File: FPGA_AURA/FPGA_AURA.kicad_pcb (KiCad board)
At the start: 8 copper layers, 50 x 50 mm, 147 parts, among them J1 TF-CARD_H1.8, J100 USB_C_Receptacle_USB2.0_16P, J101 XT30PW-M, J2 532617004, J3 532617007, J4 532617004, U1 XC7A35T-2FTG256C, U2 W25Q256JVEIQ, U200 ADP5014, U3 FT2232HQ, U4 TPS51200DRCR, U5 USBLC6-2SC6, U500 MT41K128M16JT-125_IT_K, U6 93LC56BT-I_SN, Y1 12MHz

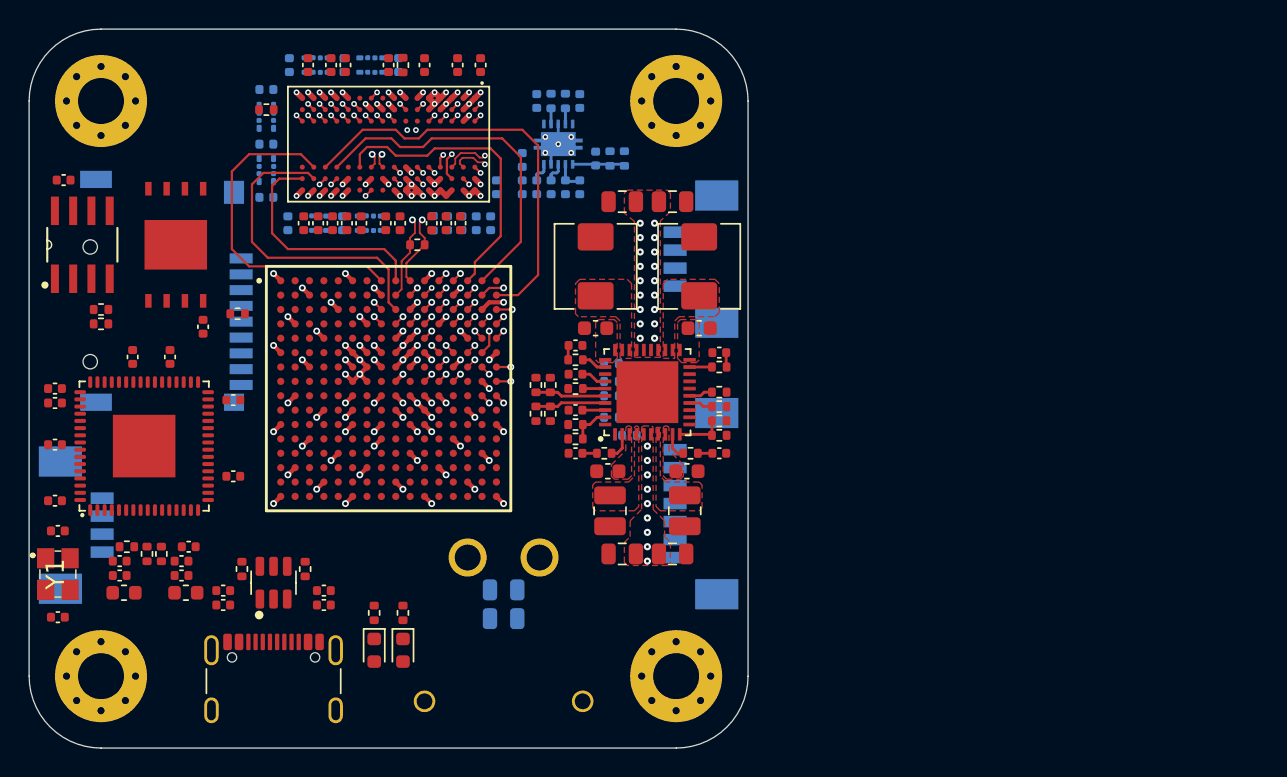
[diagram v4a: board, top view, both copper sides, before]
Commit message: Changing stackup to 10 layers and connectors change
Development has been slow due to SI concerns with 8 layers so changing the layer count to 10 will simplify design. The picoblade/SD connector(s) are large and not high speed, so a high speed mezzanine will be used to go to a daughter board with the picoblade connectors and SD card, or other devices/protocols e.g. ADCs, COAX, IMUs, etc.
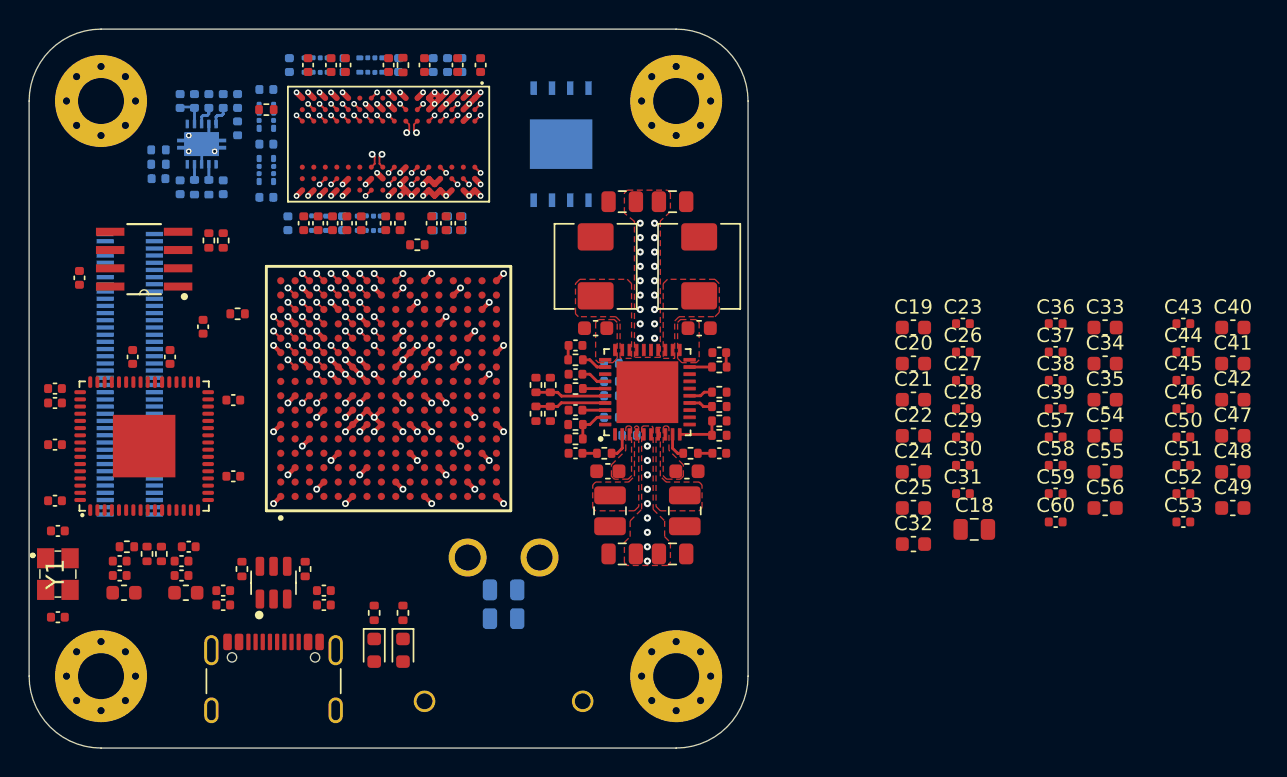
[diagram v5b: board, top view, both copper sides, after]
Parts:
- removed J2, J4: 532617004, 532617004:532617004
- removed J3: 532617007, 532617007:532617007
- added C18: 100u, Capacitor_SMD:C_0805_2012Metric, F.Cu at (165.7, 84.8)
- added C19: 4u7, Capacitor_SMD:C_0603_1608Metric, F.Cu at (161.5, 70.8)
- added C20: 4u7, Capacitor_SMD:C_0603_1608Metric, F.Cu at (161.5, 73.3)
- added C21: 4u7, Capacitor_SMD:C_0603_1608Metric, F.Cu at (161.5, 75.8)
- added C22: 4u7, Capacitor_SMD:C_0603_1608Metric, F.Cu at (161.5, 78.3)
- added C23: 470n, Capacitor_SMD:C_0402_1005Metric, F.Cu at (164.9, 70.5)
- added C24: 4u7, Capacitor_SMD:C_0603_1608Metric, F.Cu at (161.5, 80.8)
- added C25: 47, Capacitor_SMD:C_0603_1608Metric, F.Cu at (161.5, 83.3)
- added C26: 470n, Capacitor_SMD:C_0402_1005Metric, F.Cu at (164.9, 72.5)
- added C27: 470n, Capacitor_SMD:C_0402_1005Metric, F.Cu at (164.9, 74.4)
- added C28: 470n, Capacitor_SMD:C_0402_1005Metric, F.Cu at (164.9, 76.4)
- added C29: 470n, Capacitor_SMD:C_0402_1005Metric, F.Cu at (164.9, 78.4)
- added C30: 470n, Capacitor_SMD:C_0402_1005Metric, F.Cu at (164.9, 80.3)
- added C31: 470n, Capacitor_SMD:C_0402_1005Metric, F.Cu at (164.9, 82.3)
- added C32: 47, Capacitor_SMD:C_0603_1608Metric, F.Cu at (161.5, 85.8)
- added C33: 47, Capacitor_SMD:C_0603_1608Metric, F.Cu at (174.8, 70.8)
- added C34: 4u7, Capacitor_SMD:C_0603_1608Metric, F.Cu at (174.8, 73.3)
- added C35: 4u7, Capacitor_SMD:C_0603_1608Metric, F.Cu at (174.8, 75.8)
- added C36: 470n, Capacitor_SMD:C_0402_1005Metric, F.Cu at (171.4, 70.5)
- added C37: 470n, Capacitor_SMD:C_0402_1005Metric, F.Cu at (171.4, 72.5)
- added C38: 470n, Capacitor_SMD:C_0402_1005Metric, F.Cu at (171.4, 74.4)
- added C39: 470n, Capacitor_SMD:C_0402_1005Metric, F.Cu at (171.4, 76.4)
- added C40: 47, Capacitor_SMD:C_0603_1608Metric, F.Cu at (183.7, 70.8)
- added C41: 4u7, Capacitor_SMD:C_0603_1608Metric, F.Cu at (183.7, 73.3)
- added C42: 4u7, Capacitor_SMD:C_0603_1608Metric, F.Cu at (183.7, 75.8)
- added C43: 470n, Capacitor_SMD:C_0402_1005Metric, F.Cu at (180.3, 70.5)
- added C44: 470n, Capacitor_SMD:C_0402_1005Metric, F.Cu at (180.3, 72.5)
- added C45: 470n, Capacitor_SMD:C_0402_1005Metric, F.Cu at (180.3, 74.4)
- added C46: 470n, Capacitor_SMD:C_0402_1005Metric, F.Cu at (180.3, 76.4)
- added C47: 47, Capacitor_SMD:C_0603_1608Metric, F.Cu at (183.7, 78.3)
- added C48: 4u7, Capacitor_SMD:C_0603_1608Metric, F.Cu at (183.7, 80.8)
- added C49: 4u7, Capacitor_SMD:C_0603_1608Metric, F.Cu at (183.7, 83.3)
- added C50: 470n, Capacitor_SMD:C_0402_1005Metric, F.Cu at (180.3, 78.4)
- added C51: 470n, Capacitor_SMD:C_0402_1005Metric, F.Cu at (180.3, 80.3)
- added C52: 470n, Capacitor_SMD:C_0402_1005Metric, F.Cu at (180.3, 82.3)
- added C53: 470n, Capacitor_SMD:C_0402_1005Metric, F.Cu at (180.3, 84.3)
- added C54: 47, Capacitor_SMD:C_0603_1608Metric, F.Cu at (174.8, 78.3)
- added C55: 4u7, Capacitor_SMD:C_0603_1608Metric, F.Cu at (174.8, 80.8)
- added C56: 4u7, Capacitor_SMD:C_0603_1608Metric, F.Cu at (174.8, 83.3)
- added C57: 470n, Capacitor_SMD:C_0402_1005Metric, F.Cu at (171.4, 78.4)
- added C58: 470n, Capacitor_SMD:C_0402_1005Metric, F.Cu at (171.4, 80.3)
- added C59: 470n, Capacitor_SMD:C_0402_1005Metric, F.Cu at (171.4, 82.3)
- added C60: 470n, Capacitor_SMD:C_0402_1005Metric, F.Cu at (171.4, 84.3)
- J1: value TF-CARD_H1.8 -> ST5-40-1.00-L-D-P-TR; footprint TF-CARD_H1_8:TFCARDH18 -> ST5-40-1.00-L-D-P-TR:ST5-40-1.00-L-D-P-TR
- U2: moved to B.Cu
- moved R222 32.4 mm to (109.0, 58.4), turned to 0 degrees
- moved R221 31.4 mm to (109.0, 59.4), turned to 180 degrees
- moved C216 30.4 mm to (109.0, 60.4), turned to 180 degrees
- moved C217 28.4 mm to (110.5, 55.0), turned to 90 degrees
- moved C221 28.4 mm to (110.5, 61.0), turned to -90 degrees
- moved U2 27.7 mm to (137.0, 58.0)
- moved C218 26.5 mm to (111.5, 55.0), turned to 90 degrees
- moved R223 26.5 mm to (111.5, 61.0), turned to 90 degrees
- moved U4 24.8 mm to (112.0, 58.0), turned to -90 degrees
- moved C215 24.5 mm to (112.5, 55.0), turned to 90 degrees
- moved R220 24.5 mm to (112.5, 61.0), turned to 90 degrees
- moved C214 22.6 mm to (113.5, 61.0), turned to -90 degrees
- moved C219 22.6 mm to (113.5, 55.0), turned to 90 degrees
- moved C222 20.7 mm to (114.5, 55.0), turned to 90 degrees
- moved C508 19.9 mm to (114.5, 56.9), turned to -90 degrees
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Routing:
- net DDR3_ODT: track 37.4 -> 1.27 mm
- net DDR3_CS: track 36.0 -> 1.27 mm
- net DDR3_A2: track 35.9 -> 1.27 mm
- net DDR3_DQ12: track 32.3 -> 1.27 mm
- net DDR3_WE: track 30.7 -> 1.27 mm
- net DDR3_A1: track 29.3 -> 0.00 mm
- net DDR3_A5: track 30.5 -> 1.27 mm
- net DDR3_DM1: track 29.1 -> 1.27 mm
- net DDR3_DQ13: track 29.0 -> 1.27 mm
- net DDR3_A13: track 26.8 -> 1.27 mm
- net DDR3_A7: track 26.4 -> 1.27 mm
- net DDR3_DQ9: track 26.3 -> 1.27 mm
- net DDR3_CK-: track 25.5 -> 1.06 mm, vias 2 -> 1
- net DDR3_A12: track 24.4 -> 0.00 mm
- net DDR3_CK+: track 25.3 -> 1.06 mm, vias 2 -> 1
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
